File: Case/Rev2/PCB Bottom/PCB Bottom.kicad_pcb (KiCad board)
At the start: 2 copper layers, 147.3 x 89 mm, 7 parts

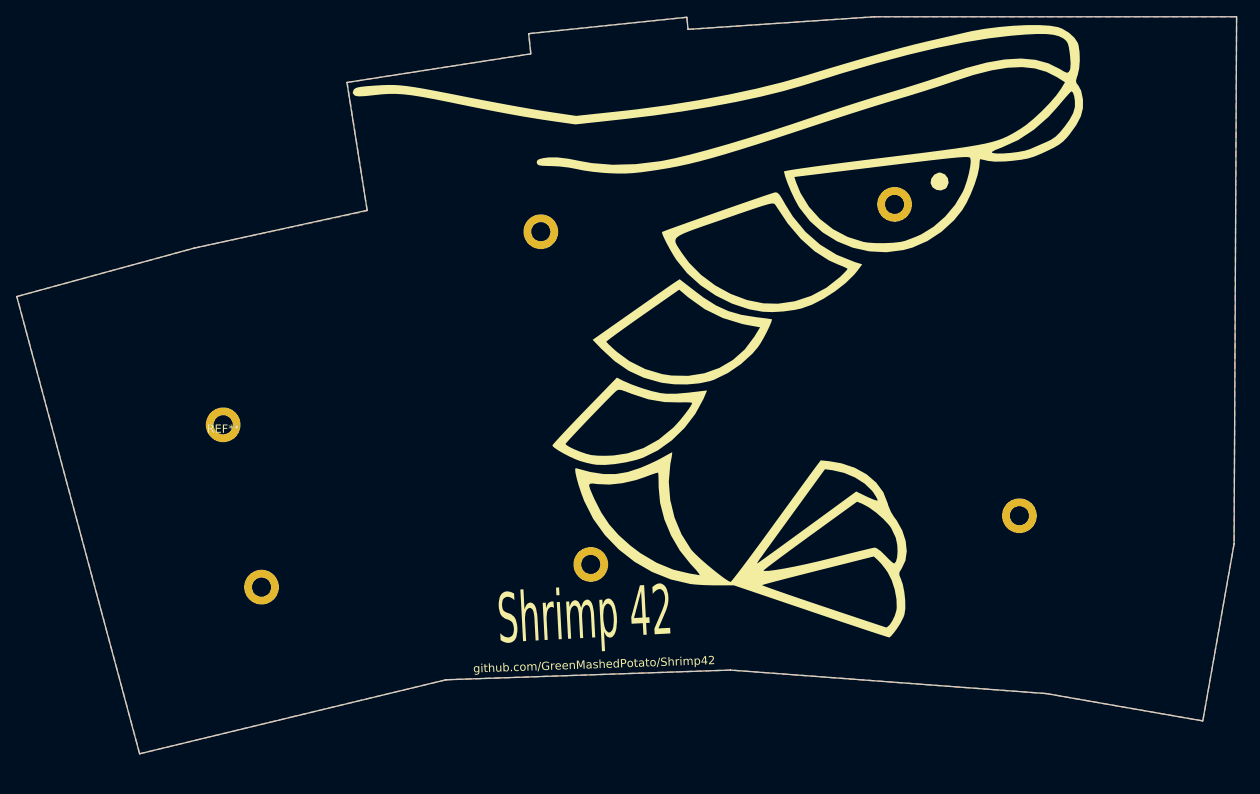
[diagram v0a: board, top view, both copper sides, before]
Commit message: update thumb cluster since its too close to amphenol cutout
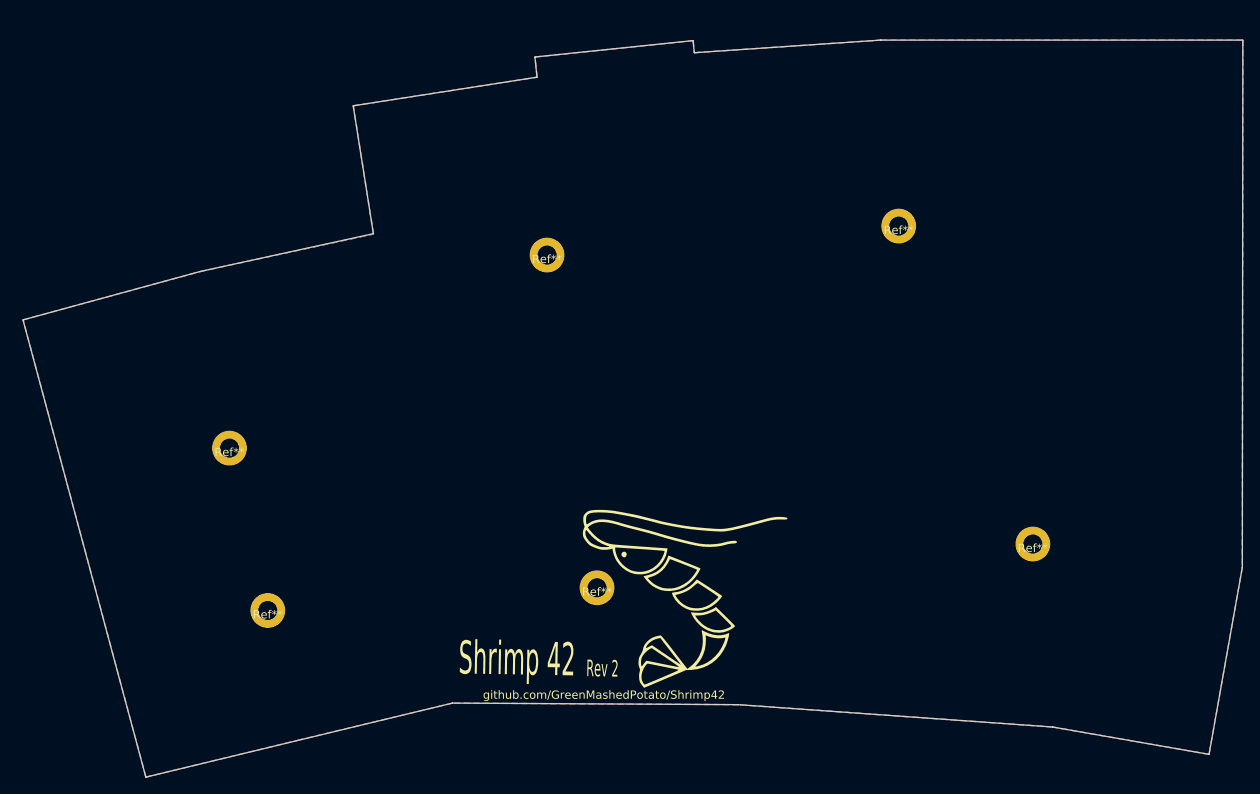
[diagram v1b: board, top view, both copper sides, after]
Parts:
- removed ? (x5): , 
- removed the G*** at (106.0, 64.3)
- removed REF**: M2_Hole_TH, Footprints:hole-m2
- added G***: LOGO, footprints:Shrimp_small_small, F.Cu at (93.5, 87.0)
- added Ref**: Val**, footprints:hole-m2, F.Cu at (77.7, 43.9)
- added Ref**: Val**, footprints:hole-m2, F.Cu at (136.4, 78.8)
- added Ref**: Val**, footprints:hole-m2, F.Cu at (83.8, 84.1)
- added Ref**: Val**, footprints:hole-m2, F.Cu at (39.4, 67.2)
- added Ref**: Val**, footprints:hole-m2, F.Cu at (44.0, 86.8)
- added Ref**: Val**, footprints:hole-m2, F.Cu at (120.2, 40.4)
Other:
- outline, holes or cut-outs redrawn
- board text added: "Rev 2"
